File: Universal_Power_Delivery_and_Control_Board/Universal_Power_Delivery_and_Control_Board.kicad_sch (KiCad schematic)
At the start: 0 parts

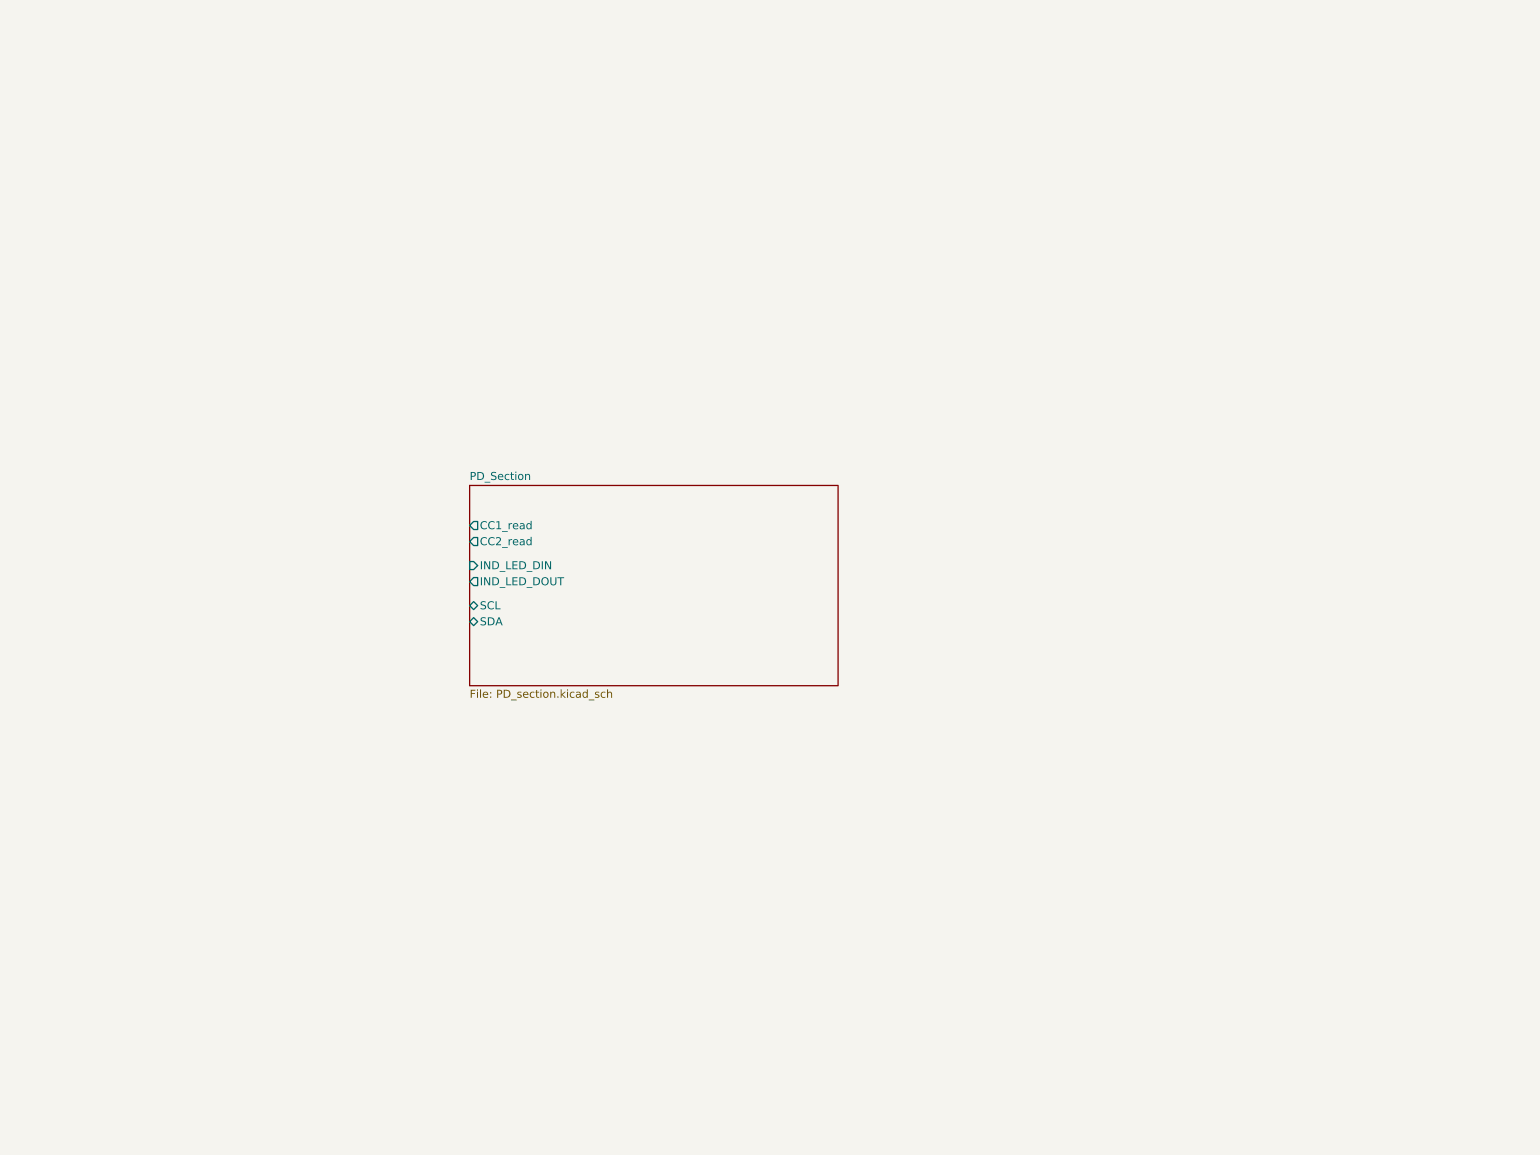
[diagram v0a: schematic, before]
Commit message: Continued with routing on the UPDC and minor changes on the matrix board.
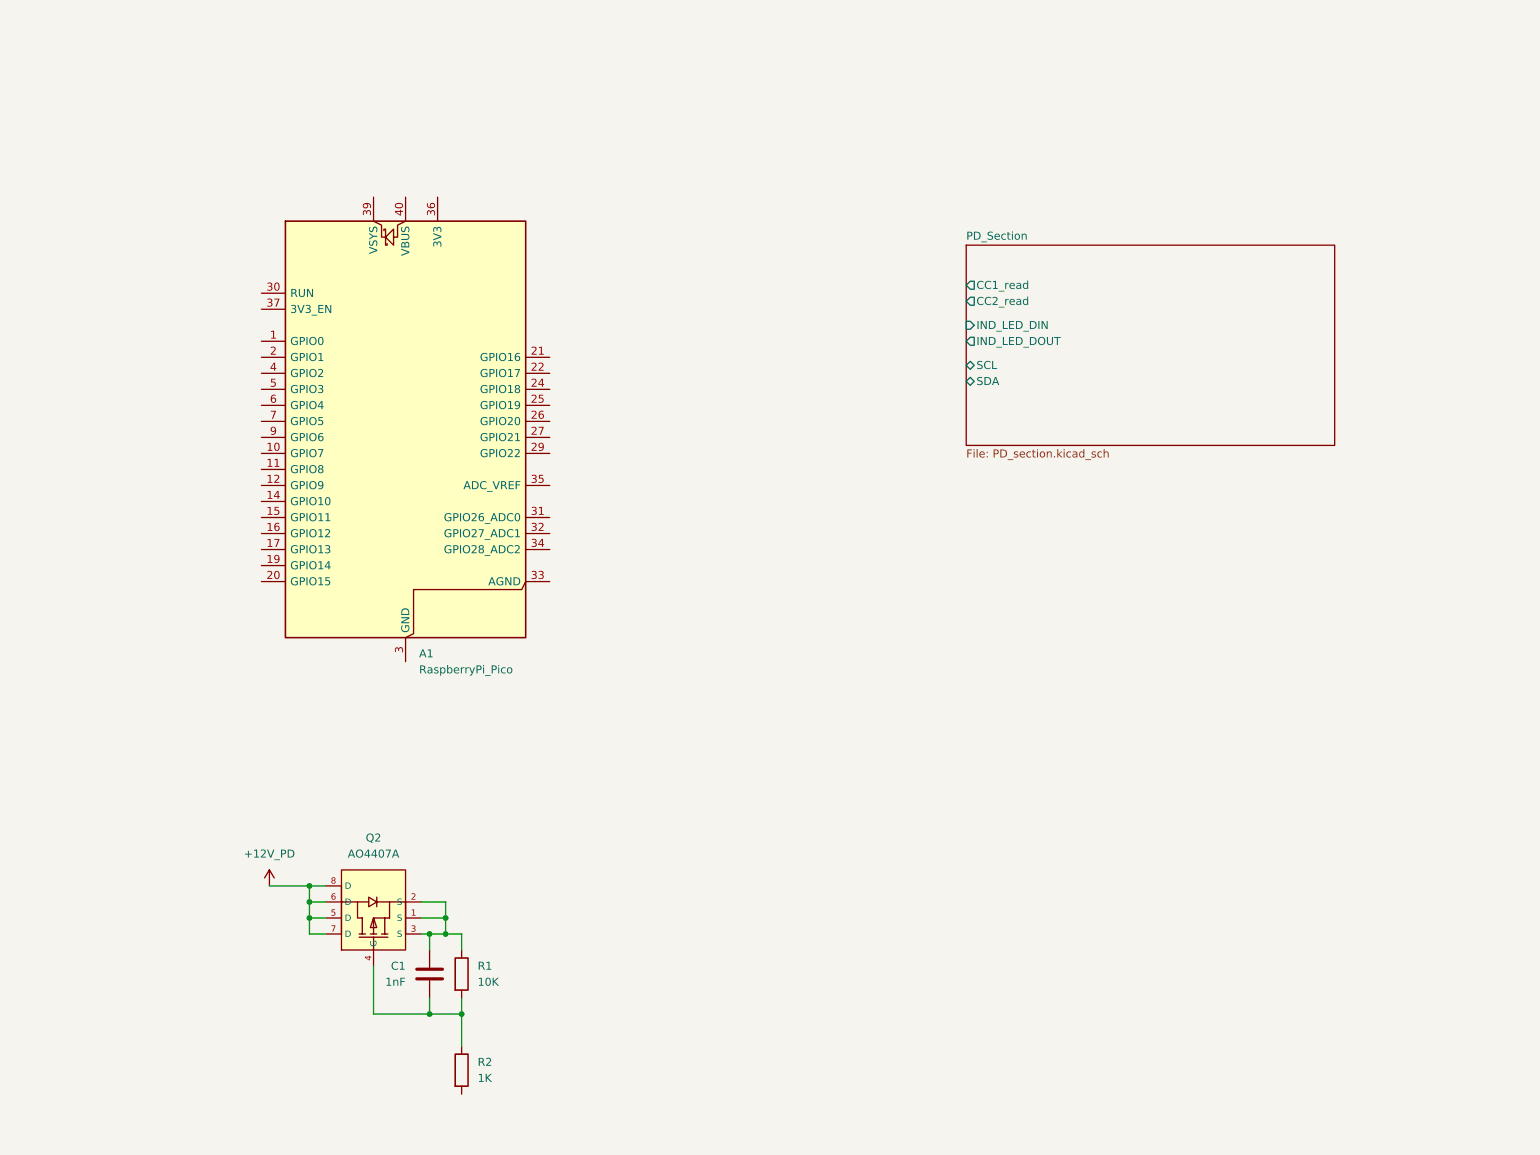
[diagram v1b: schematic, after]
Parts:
- added A1: RaspberryPi_Pico, Module:RaspberryPi_Pico_Common_Unspecified, symbol MCU_Module:RaspberryPi_Pico
- added C1: 1nF, Capacitor_SMD:C_0402_1005Metric_Pad0.74x0.62mm_HandSolder, symbol Device:C
- added Q2: AO4407A, lcsc_footprints:C16072_SOIC-8_L4_9-W3_9-P1_27-LS6_0-BL, symbol lcsc_imported:AO4407A
- added R1: 10K, Resistor_SMD:R_0402_1005Metric_Pad0.72x0.64mm_HandSolder, symbol Device:R
- added R2: 1K, Resistor_SMD:R_0402_1005Metric_Pad0.72x0.64mm_HandSolder, symbol Device:R
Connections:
- new net: C1.1, Q2.1 (S), Q2.2 (S), Q2.3 (S), R1.1
- new net: C1.2, Q2.4 (G), R1.2, R2.1
- new net: A1.13 (GND), A1.18 (GND), A1.23 (GND), A1.28 (GND), A1.3 (GND), A1.38 (GND), A1.8 (GND)
- new net +12V_PD: Q2.5 (D), Q2.6 (D), Q2.7 (D), Q2.8 (D)

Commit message: Imported the buck converter design block and contnued with the layout.
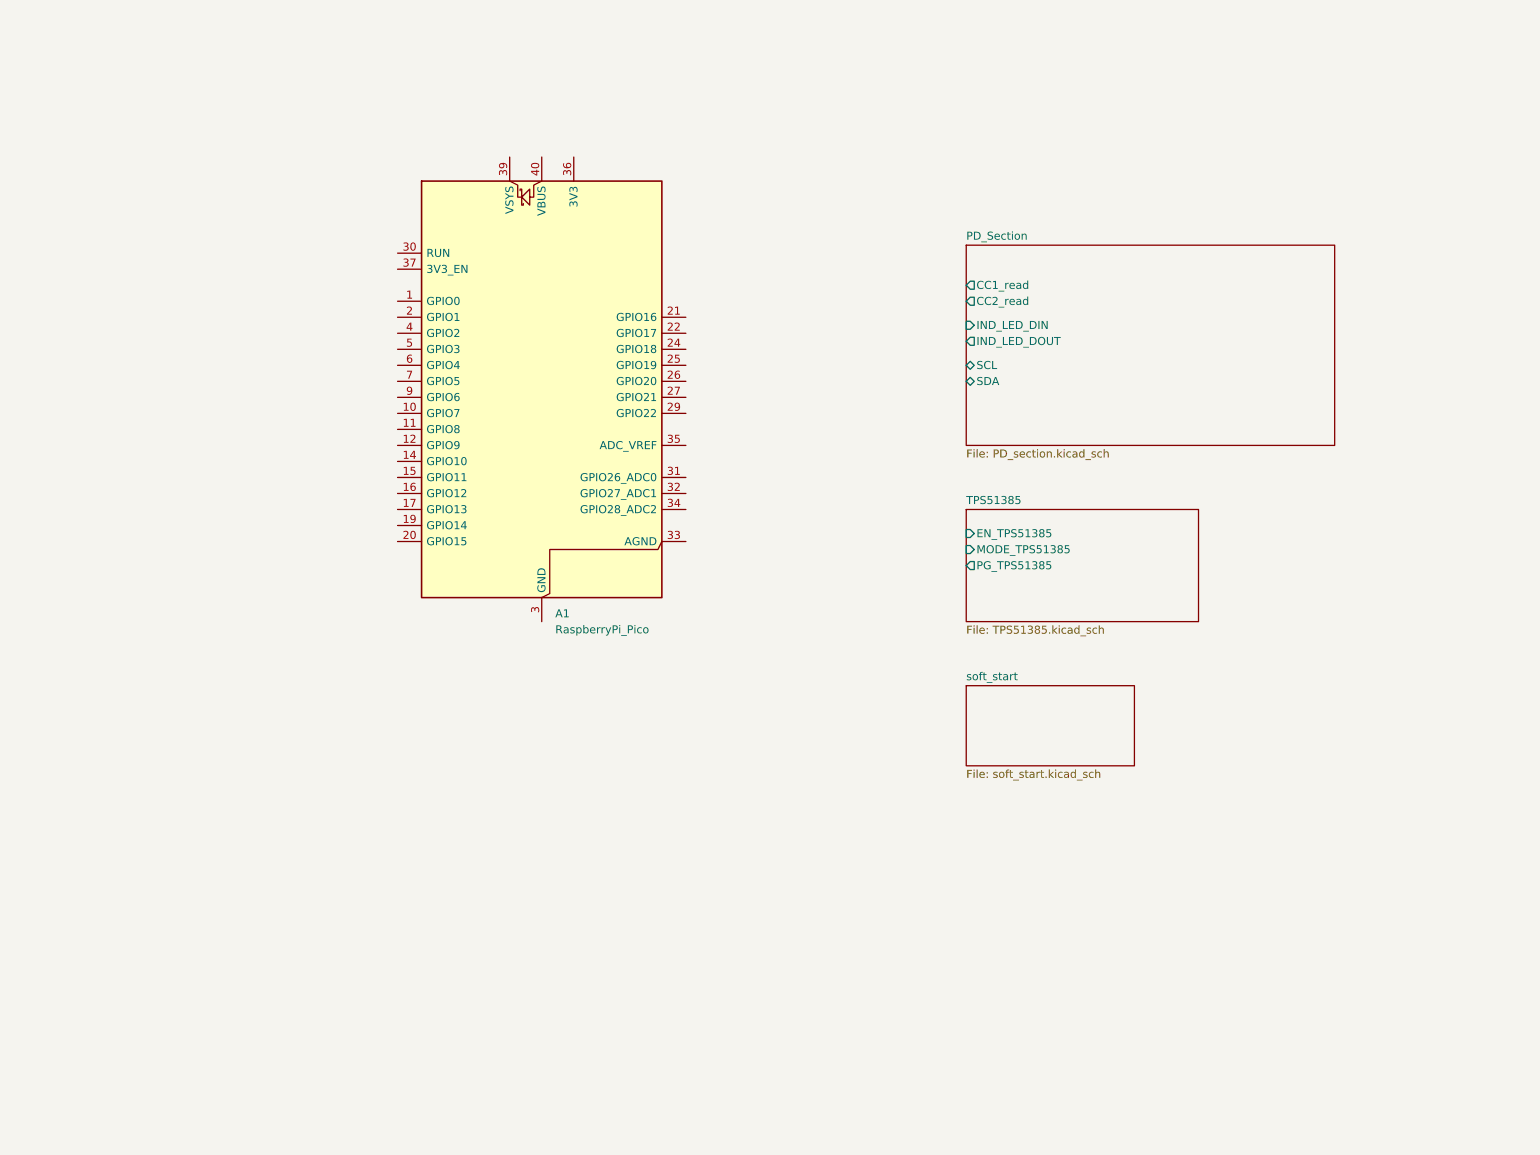
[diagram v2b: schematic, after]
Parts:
- removed C1: 1nF, Capacitor_SMD:C_0402_1005Metric_Pad0.74x0.62mm_HandSolder, symbol Device:C
- removed Q2: AO4407A, lcsc_footprints:C16072_SOIC-8_L4_9-W3_9-P1_27-LS6_0-BL, symbol lcsc_imported:AO4407A
- removed R1: 10K, Resistor_SMD:R_0402_1005Metric_Pad0.72x0.64mm_HandSolder, symbol Device:R
- removed R2: 1K, Resistor_SMD:R_0402_1005Metric_Pad0.72x0.64mm_HandSolder, symbol Device:R
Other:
- added sheet TPS51385 (TPS51385.kicad_sch)
- added sheet soft_start (soft_start.kicad_sch)
- moved on the sheet: A1

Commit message: Finally figured out the soft start circuitry.
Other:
- sheet TPS51385 renamed Power_Output
- removed sheet soft_start
- sheet Power_Output ports: added SOFT_START_EN; removed none
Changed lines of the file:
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@@
-	)
-	(sheet
-		(at 184.15 119.38)
-		(size 26.67 12.7)
-		(exclude_from_sim no)
-		(in_bom yes)
-		(on_board yes)
-		(dnp no)
-		(fields_autoplaced yes)
-		(stroke
-			(width 0.1524)
-			(type solid)
-		)
-		(fill
-			(color 0 0 0 0)
-		)
-		(property "Sheetname" "soft_start"
-			(at 184.15 118.6684 0)
-			(show_name no)
-			(do_not_autoplace no)
-			(effects
-				(font
-					(size 1.27 1.27)
-				)
-				(justify left bottom)
-			)
-		)
-		(property "Sheetfile" "soft_start.kicad_sch"
-			(at 184.15 132.6646 0)
-			(show_name no)
-			(do_not_autoplace no)
-			(effects
-				(font
-					(size 1.27 1.27)
-				)
-				(justify left top)
-			)
-		)
-		(instances
-			(project "Universal_Power_Delivery_and_Control_Board"
-				(path "/b749dd2f-6b66-411b-a989-65da6091f700"
-					(page "4")
-				)
-			)
-		)
 	)
 	(sheet
@@
 			(color 0 0 0 0)
 		)
-		(property "Sheetname" "TPS51385"
+		(property "Sheetname" "Power_Output"
 			(at 184.15 90.7284 0)
 			(show_name no)
@@
 			(effects
 				(font
+					(size 1.27 1.27)
+				)
+				(justify left)
+			)
+		)
+		(pin "SOFT_START_EN" input
+			(at 184.15 105.41 180)
+			(effects
+				(font
